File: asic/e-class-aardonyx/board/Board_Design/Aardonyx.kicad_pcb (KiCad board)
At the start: 4 copper layers, 306 parts, among them J1 USB_B_6PIN, J10 Conn_1x6_F, J11 Conn_1x6_F, J12 Conn_1x3_M, J13 Conn_1x8_F, J14 Conn_1x6_F, J15 Conn_1x10, J16 Conn_1x8_F, J17 USB_OTG, J18 Conn_1x3_M, J19 Conn_1x3_M, J2 Conn_1x8, J3 Conn_1x3_M, J4 Conn_1x4, J5 PJ-202H PWRJACK, J6 Conn_1x3_M, J7 Conn_1x4, J8 Conn_1x3_M, J9 Conn_1x8, Q1 FDN339AN, SW1 SW_SPST, SW2 FSM2JSMAATR, SW3 SW_DIP_x03, U1 FT2232H, U10 TPS7A7002DDAR, U11 ADM1085, U12 ADM1085, U13 TPS7A7002DDAR, U14 74AUP1G09GW, U15 SKT32E, U16 93LC56BT-I_OT, U2 IS42S32160F-TSOP2, U3 CDCE913PW, U4 TPS54627DDAR, U5 CAT24M01WI-GT3, U6 IS25LP256x-xM, U7 ADC128S102CIMTX/NOPB, U8 LSF0108PWR, U9 LSF0108PWR, Y1 12MHz, Y2 27MHz

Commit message: updated the component
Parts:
- C11, C13, C14, C15, C16, C17: moved to B.Cu
- H1, H2, H3, H4, H5, H6: footprint MountingHole:MountingHole_3.5mm_Pad_Via -> MountingHole:MountingHole_3.2mm_M3
- moved H2 245.6 mm to (275.0, 25.0)
- moved H4 227.6 mm to (275.0, 154.0)
- moved H1 134.6 mm to (176.4, 121.0)
- moved H3 96.2 mm to (114.0, 25.0)
- moved H5 84.2 mm to (124.3, 154.0)
- moved H6 71.5 mm to (114.0, 155.0)
- moved FID1 70.1 mm to (114.9, 45.3)
- moved FID2 58.6 mm to (117.5, 131.6)
- moved R19 55.4 mm to (203.8, 103.3), turned to 0 degrees
- moved R20 53.6 mm to (203.8, 104.6), turned to 0 degrees
- moved TP2 52.9 mm to (218.7, 29.7)
- moved R1 32.5 mm to (212.3, 60.9)
- moved C17 31.2 mm to (222.7, 53.5), turned to 270 degrees
- moved J15 29.6 mm to (151.9, 105.4)
- moved C53 29.1 mm to (142.3, 128.3)
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
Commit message: Added few components
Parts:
- added C93: 0.1UF,0402, Capacitor_SMD:C_0402_1005Metric, F.Cu at (217.2, 116.0)
- added C94: 0.1UF,0402, Capacitor_SMD:C_0402_1005Metric, F.Cu at (218.7, 127.6)
- added FB6: 47E,FB,0402, Inductor_SMD:L_0402_1005Metric, F.Cu at (267.6, 41.0)
- added FB7: 47E,FB,0402, Inductor_SMD:L_0402_1005Metric, F.Cu at (275.7, 66.4)
- added H7: MountingHole, MountingHole:MountingHole_3.2mm_M3, F.Cu at (116.8, 116.8)
- R128, R129, R130, R30, R31, R32, R33, R34, R35, R48, R51, R55: value 10KE,0805 -> 10KE,0402
- moved J10 93.5 mm to (230.1, 50.8), turned to 0 degrees
- moved SW3 88.1 mm to (255.0, 149.9), turned to 270 degrees
- moved R130 87.0 mm to (255.6, 145.0), turned to 90 degrees
- moved R132 85.8 mm to (246.4, 157.5), turned to 0 degrees
- moved R129 82.4 mm to (252.3, 144.9), turned to 90 degrees
- moved R131 82.4 mm to (246.4, 156.0), turned to 0 degrees
- moved R32 82.0 mm to (224.5, 54.4), turned to 270 degrees
- moved U6 81.0 mm to (212.6, 58.4)
- moved R30 79.2 mm to (221.0, 63.0), turned to 180 degrees
- moved R128 78.2 mm to (249.4, 144.8), turned to 90 degrees
- moved J8 72.9 mm to (213.9, 49.8)
- moved J2 72.0 mm to (203.2, 94.0)
- moved C48 72.0 mm to (205.0, 54.9)
- moved J3 63.6 mm to (270.1, 78.7), turned to 0 degrees
- moved R31 62.7 mm to (204.7, 52.3), turned to 270 degrees
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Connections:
- C56 pad 1: V3P3 -> Net-(C56-Pad1)
- C62 pad 1: V1P8 -> Net-(C62-Pad1)
- J1 pad 5: GND -> Net-(FB6-Pad1)
- J10 pad 1: /soc/SPI1_CLK -> /arduino_header/SPI1_nCS
- J17 pad 6: GND -> Net-(FB7-Pad2)
- P_R1 pad 2: Net-(P_R1-Pad2) -> Net-(C56-Pad1)
- P_R2 pad 2: Net-(P_R2-Pad2) -> Net-(C62-Pad1)
- P_R41 pad 1: Net-(P_R1-Pad2) -> Net-(C56-Pad1)
- P_R49 pad 1: Net-(P_R2-Pad2) -> Net-(C62-Pad1)
- R128 pad 1: /soc/TEST_MODE -> /soc/BOOT_MODE0
- R130 pad 1: /soc/BOOT_MODE0 -> /soc/TEST_MODE
- R61 pad 2: /arduino_header/SPI1_CLK -> /arduino_header/SPI1_nCS
- R62 pad 2: /soc/SPI1_CLK -> /arduino_header/SPI1_CLK
- SW3 pad 1: /soc/BOOT_MODE0 -> /soc/TEST_MODE
- SW3 pad 3: /soc/TEST_MODE -> /soc/BOOT_MODE0
- U10 pad 6: Net-(P_R1-Pad2) -> Net-(C56-Pad1)
- U13 pad 6: Net-(P_R2-Pad2) -> Net-(C62-Pad1)

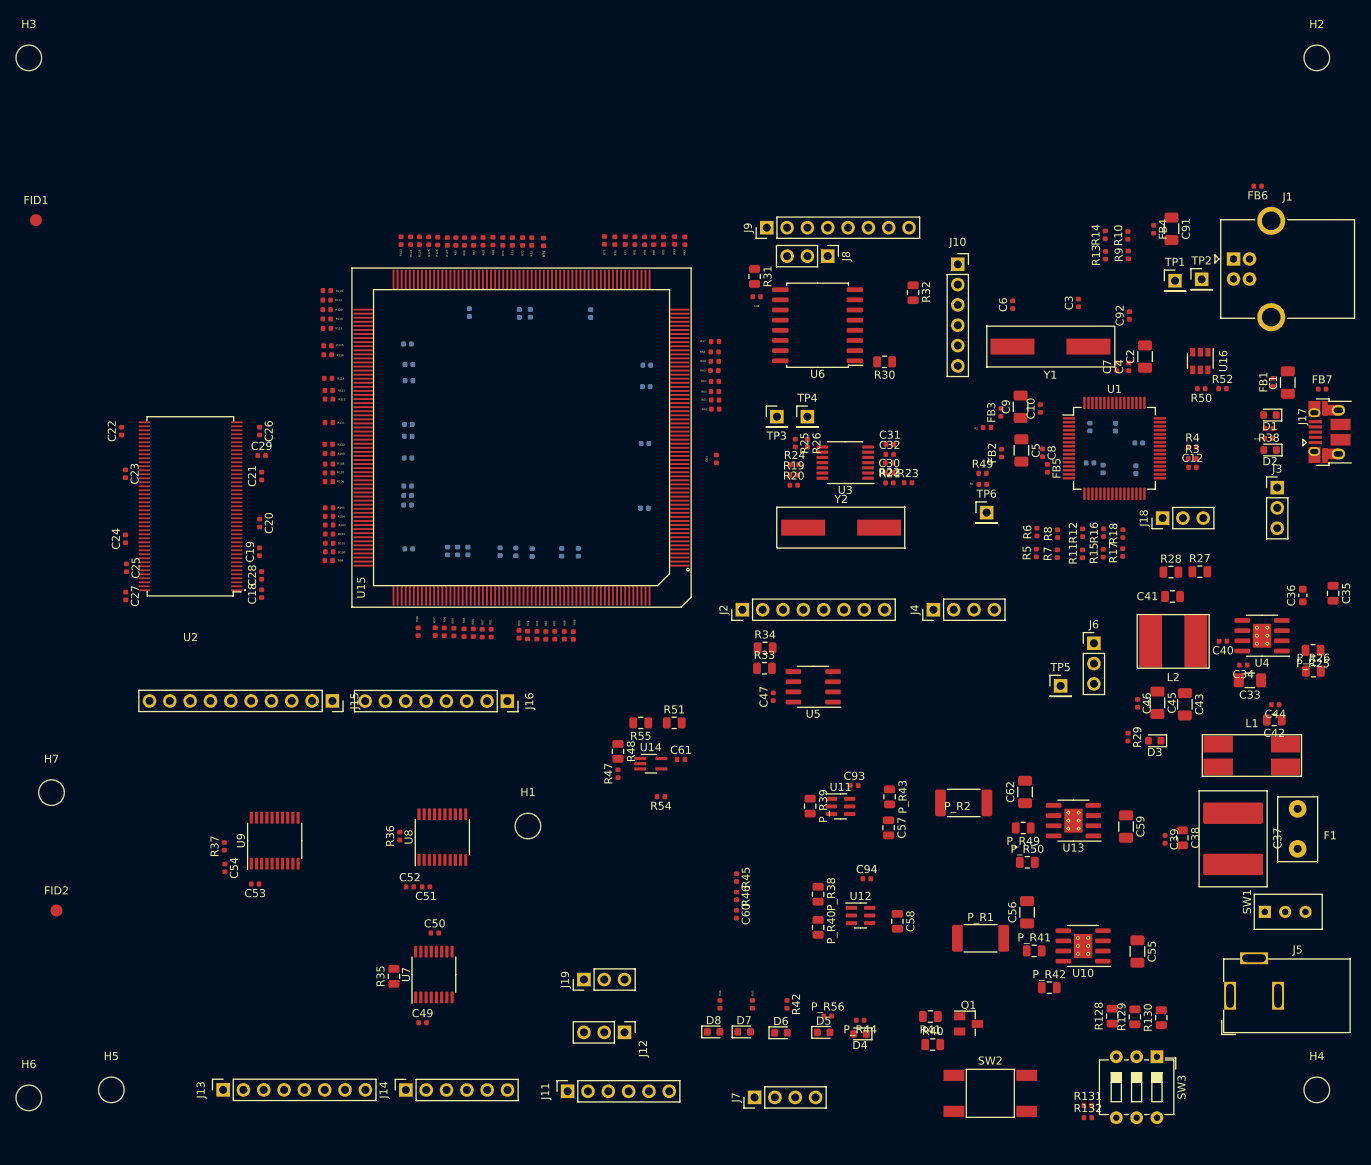
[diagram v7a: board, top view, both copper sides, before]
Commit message: pcb size minimised
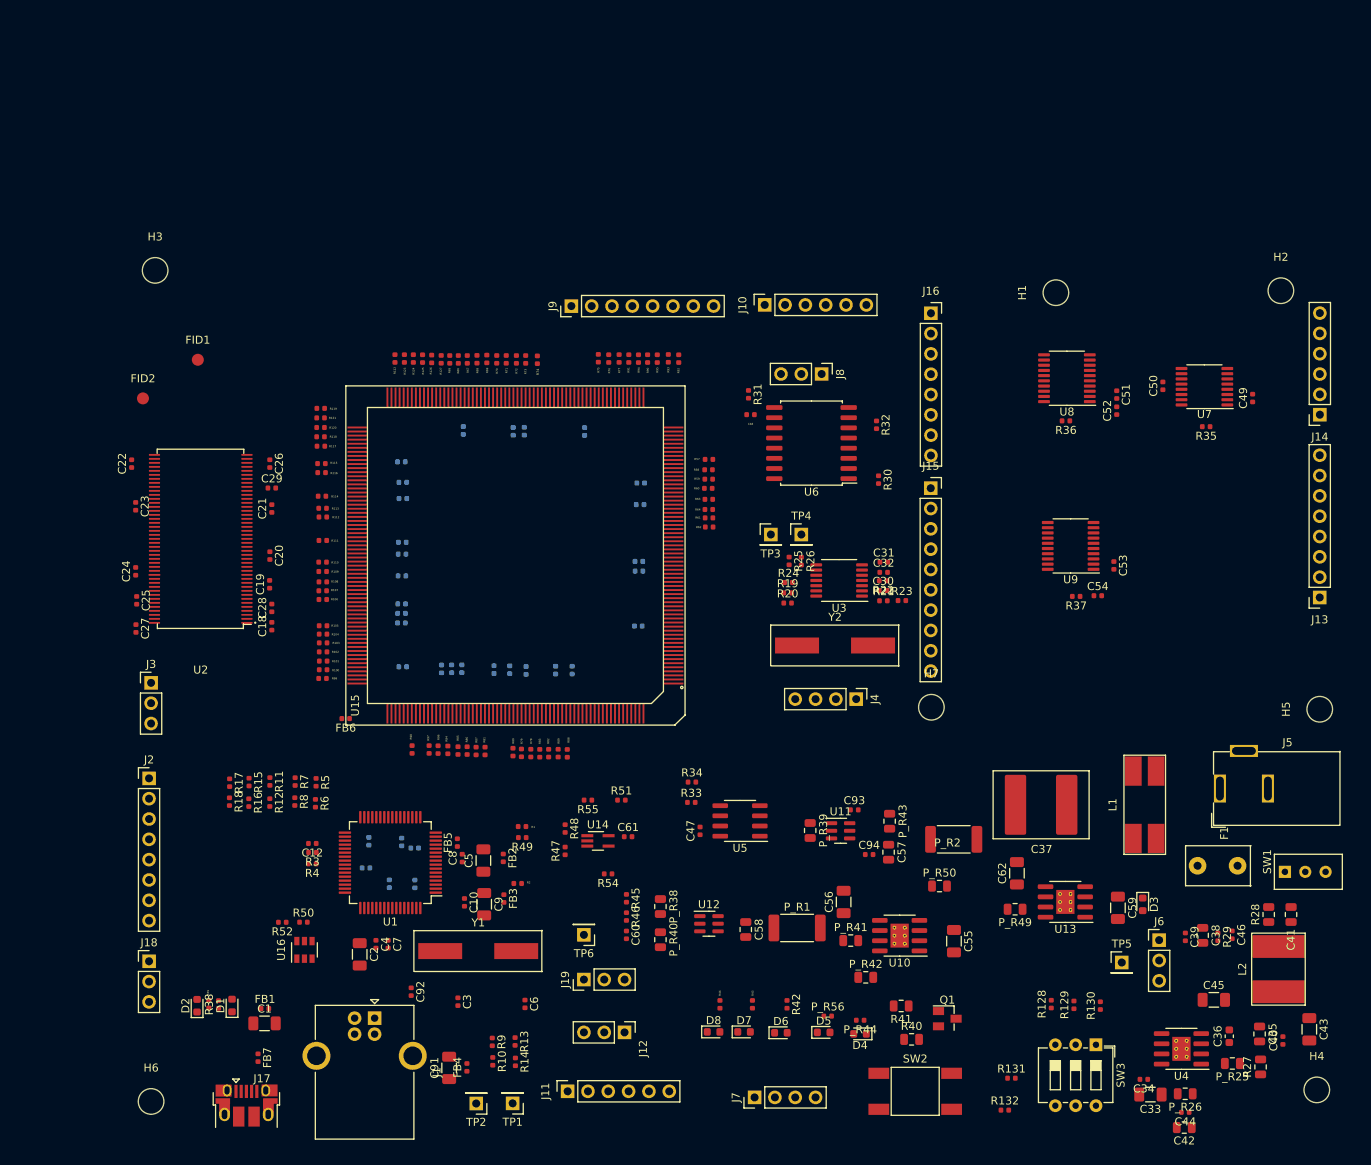
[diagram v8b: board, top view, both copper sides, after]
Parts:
- C63: moved to B.Cu
- R128, R129, R130, R30, R31, R32, R33, R34, R35, R48, R51, R55: footprint Resistor_SMD:R_0805_2012Metric -> Resistor_SMD:R_0402_1005Metric
- moved J17 159.4 mm to (141.2, 156.0), turned to 0 degrees
- moved H5 158.4 mm to (275.4, 106.4), turned to 90 degrees
- moved FB7 157.1 mm to (142.7, 150.0), turned to 270 degrees
- moved D2 151.0 mm to (135.0, 143.5), turned to 90 degrees
- moved C1 150.9 mm to (143.5, 145.7), turned to 0 degrees
- moved J13 150.3 mm to (275.4, 92.5), turned to 180 degrees
- moved R39 150.2 mm to (136.5, 143.3), turned to 90 degrees
- moved R38 149.7 mm to (137.7, 143.3), turned to 90 degrees
- moved D1 149.3 mm to (139.4, 143.5), turned to 90 degrees
- moved FB1 148.3 mm to (143.5, 143.8), turned to 0 degrees
- moved J1 143.3 mm to (157.2, 145.0), turned to 270 degrees
- moved J3 142.9 mm to (129.3, 103.1)
- moved J14 142.0 mm to (275.4, 69.6), turned to 180 degrees
- moved C91 138.4 mm to (166.5, 151.3), turned to 90 degrees
- moved J18 138.3 mm to (129.0, 137.9), turned to 0 degrees
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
